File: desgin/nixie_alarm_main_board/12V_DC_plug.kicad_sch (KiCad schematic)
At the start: 4 parts, among them J1 DCPLUG 2x6.4mm 2A

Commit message: new caps footprint
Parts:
- C22: footprint GRM033D70J224ME01D -> Capacitor_SMD:C_0805_2012Metric_Pad1.18x1.45mm_HandSolder
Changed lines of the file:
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@@
 			)
 		)
-		(property "Footprint" "GRM033D70J224ME01D"
+		(property "Footprint" "Capacitor_SMD:C_0805_2012Metric_Pad1.18x1.45mm_HandSolder"
 			(at 282.372 81.534 0)
 			(effects

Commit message: new board v1
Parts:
- removed J1: DCPLUG 2x6.4mm 2A, DCJ20005AK1A, symbol SamacSys_Parts:DCJ200-05-A-K1-A
- added J1: PJ-094H-SMT-TR, PJ094HSMTTR, symbol SamacSys_Parts:PJ-094H-SMT-TR
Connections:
- net +12V: now also J1.1
- net GND: now also J1.2, J1.3
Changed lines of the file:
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@@
-	)
-	(junction
-		(at 104.14 93.472)
-		(diameter 0)
-		(color 0 0 0 0)
 	)
 	(junction
@@
 	)
 	(junction
-		(at 105.41 70.612)
+		(at 103.886 86.106)
 		(diameter 0)
 		(color 0 0 0 0)
@@
 	(wire
 		(pts
+			(xy 102.87 70.612) (xy 102.87 81.026)
+		)
+		(stroke
+			(width 0)
+			(type default)
+		)
+	)
+	(wire
+		(pts
 			(xy 143.002 70.612) (xy 143.002 77.978)
 		)
@@
 	(wire
 		(pts
-			(xy 102.87 70.612) (xy 105.41 70.612)
-		)
-		(stroke
-			(width 0)
-			(type default)
-		)
-	)
-	(wire
-		(pts
-			(xy 105.41 70.612) (xy 143.002 70.612)
+			(xy 102.87 70.612) (xy 143.002 70.612)
+		)
+		(stroke
+			(width 0)
+			(type default)
+		)
+	)
+	(wire
+		(pts
+			(xy 102.87 81.026) (xy 103.886 81.026)
 		)
 		(stroke
@@
 	(wire
 		(pts
-			(xy 104.14 93.472) (xy 105.41 93.472)
+			(xy 103.886 83.566) (xy 103.886 86.106)
 		)
 		(stroke
@@
 	(wire
 		(pts
+			(xy 103.886 86.106) (xy 103.886 93.472)
+		)
+		(stroke
+			(width 0)
+			(type default)
+		)
+	)
+	(wire
+		(pts
 			(xy 165.1 70.612) (xy 143.002 70.612)
 		)
@@
 		(pts
 			(xy 186.182 90.424) (xy 186.182 104.14)
-		)
-		(stroke
-			(width 0)
-			(type default)
-		)
-	)
-	(wire
-		(pts
-			(xy 102.87 93.472) (xy 104.14 93.472)
 		)
 		(stroke
@@
 	)
 	(symbol
-		(lib_id "SamacSys_Parts:DCJ200-05-A-K1-A")
-		(at 105.41 70.612 270)
-		(unit 1)
-		(exclude_from_sim no)
-		(in_bom yes)
-		(on_board yes)
-		(dnp no)
-		(fields_autoplaced yes)
-		(property "Reference" "J1"
-			(at 109.22 80.7719 90)
-			(effects
-				(font
-					(size 1.27 1.27)
-				)
-				(justify left)
-			)
-		)
-		(property "Value" "DCPLUG 2x6.4mm 2A"
-			(at 109.22 83.3119 90)
-			(effects
-				(font
-					(size 1.27 1.27)
-				)
-				(justify left)
-			)
-		)
-		(property "Footprint" "DCJ20005AK1A"
-			(at 10.49 89.662 0)
-			(effects
-				(font
-					(size 1.27 1.27)
-				)
-				(justify left top)
-				(hide yes)
-			)
-		)
-		(property "Datasheet" "https://componentsearchengine.com/Datasheets/2/DCJ200-05-A-K1-A.pdf"
-			(at -89.51 89.662 0)
-			(effects
-				(font
-					(size 1.27 1.27)
-				)
-				(justify left top)
-				(hide yes)
-			)
-		)
-		(property "Description" "DCJ200 Series 20 V 5 A 2 Conductors/3 Contacts Horizontal SMT DC Power Jack"
-			(at 105.41 70.612 0)
-			(effects
-				(font
-					(size 1.27 1.27)
-				)
-				(hide yes)
-			)
-		)
-		(property "Height" "11.3"
-			(at -289.51 89.662 0)
-			(effects
-				(font
-					(size 1.27 1.27)
-				)
-				(justify left top)
-				(hide yes)
-			)
-		)
-		(property "Mouser Part Number" "640-DCJ200-05-A-K1-A"
-			(at -389.51 89.662 0)
-			(effects
-				(font
-					(size 1.27 1.27)
-				)
-				(justify left top)
-				(hide yes)
-			)
-		)
-		(property "Mouser Price/Stock" "https://www.mouser.co.uk/ProductDetail/GCT/DCJ200-05-A-K1-A?qs=KUoIvG%2F9IlZdgC%252BD5EAHVw%3D%3D"
-			(at -489.51 89.662 0)
-			(effects
-				(font
-					(size 1.27 1.27)
-				)
-				(justify left top)
-				(hide yes)
-			)
-		)
-		(property "Manufacturer_Name" "GCT (GLOBAL CONNECTOR TECHNOLOGY)"
-			(at -589.51 89.662 0)
-			(effects
-				(font
-					(size 1.27 1.27)
-				)
-				(justify left top)
-				(hide yes)
-			)
-		)
-		(property "Manufacturer_Part_Number" "DCJ200-05-A-K1-A"
-			(at -689.51 89.662 0)
-			(effects
-				(font
-					(size 1.27 1.27)
-				)
-				(justify left top)
-				(hide yes)
-			)
-		)
-		(pin "2"
-		)
-		(pin "4"
-		)
-		(pin "3"
-		)
-		(pin "1"
-		)
-		(instances
-			(project "nixie_alarm_main_board"
-				(path "/a0d555d7-39a0-4a98-b831-70d97d0aa5a1/3f162d9f-7cb0-459b-831b-ac42fb433594"
-					(reference "J1")
-					(unit 1)
-				)
-			)
-		)
-	)
-	(symbol
 		(lib_id "power:GND")
 		(at 186.182 104.14 0)
@@
 	)
 	(symbol
+		(lib_id "SamacSys_Parts:PJ-094H-SMT-TR")
+		(at 103.886 81.026 0)
+		(unit 1)
+		(exclude_from_sim no)
+		(in_bom yes)
+		(on_board yes)
+		(dnp no)
+		(fields_autoplaced yes)
+		(property "Reference" "J1"
+			(at 115.316 73.914 0)
+			(effects
+				(font
+					(size 1.27 1.27)
+				)
+			)
+		)
+		(property "Value" "PJ-094H-SMT-TR"
+			(at 115.316 76.454 0)
+			(effects
+				(font
+					(size 1.27 1.27)
+				)
+			)
+		)
+		(property "Footprint" "PJ094HSMTTR"
+			(at 122.936 175.946 0)
+			(effects
+				(font
+					(size 1.27 1.27)
+				)
+				(justify left top)
+				(hide yes)
+			)
+		)
+		(property "Datasheet" "https://www.cuidevices.com/product/resource/digikeypdf/pj-094h-smt-tr.pdf"
+			(at 122.936 275.946 0)
+			(effects
+				(font
+					(size 1.27 1.27)
+				)
+				(justify left top)
+				(hide yes)
+			)
+		)
+		(property "Description" "DC Power Connectors power jack, 0.65 x 2.75 mm, horizontal, SMT, high current, 1 switch, w/ shielding, T&R package"
+			(at 103.886 81.026 0)
+			(effects
+				(font
+					(size 1.27 1.27)
+				)
+				(hide yes)
+			)
+		)
+		(property "Height" "3.7"
+			(at 122.936 475.946 0)
+			(effects
+				(font
+					(size 1.27 1.27)
+				)
+				(justify left top)
+				(hide yes)
+			)
+		)
+		(property "Mouser Part Number" "490-PJ-094H-SMT-TR"
+			(at 122.936 575.946 0)
+			(effects
+				(font
+					(size 1.27 1.27)
+				)
+				(justify left top)
+				(hide yes)
+			)
+		)
+		(property "Mouser Price/Stock" "https://www.mouser.co.uk/ProductDetail/CUI-Devices/PJ-094H-SMT-TR?qs=l7cgNqFNU1iCmsfPShkP7A%3D%3D"
+			(at 122.936 675.946 0)
+			(effects
+				(font
+					(size 1.27 1.27)
+				)
+				(justify left top)
+				(hide yes)
+			)
+		)
+		(property "Manufacturer_Name" "Same Sky"
+			(at 122.936 775.946 0)
+			(effects
+				(font
+					(size 1.27 1.27)
+				)
+				(justify left top)
+				(hide yes)
+			)
+		)
+		(property "Manufacturer_Part_Number" "PJ-094H-SMT-TR"
+			(at 122.936 875.946 0)
+			(effects
+				(font
+					(size 1.27 1.27)
+				)
+				(justify left top)
+				(hide yes)
+			)
+		)
+		(pin "1"
+		)
+		(pin "2"
+		)
+		(pin "MP1"
+		)
+		(pin "3"
+		)
+		(pin "MP2"
+		)
+		(instances
+			(project "nixie_alarm_main_board"
+				(path "/a0d555d7-39a0-4a98-b831-70d97d0aa5a1/3f162d9f-7cb0-459b-831b-ac42fb433594"
+					(reference "J1")
+					(unit 1)
+				)
+			)
+		)
+	)
+	(symbol
 		(lib_id "power:GND")
 		(at 143.002 104.14 0)
@@
 	(symbol
 		(lib_id "power:GND")
-		(at 104.14 93.472 0)
+		(at 103.886 93.472 0)
 		(unit 1)
 		(exclude_from_sim no)
@@
 		(fields_autoplaced yes)
 		(property "Reference" "#PWR050"
-			(at 104.14 99.822 0)
+			(at 103.886 99.822 0)
 			(effects
 				(font
@@
 		)
 		(property "Value" "GND"
-			(at 104.14 98.552 0)
+			(at 103.886 98.552 0)
 			(effects
 				(font
@@
 		)
 		(property "Footprint" ""
-			(at 104.14 93.472 0)
+			(at 103.886 93.472 0)
 			(effects
 				(font
@@
 		)
 		(property "Datasheet" ""
-			(at 104.14 93.472 0)
+			(at 103.886 93.472 0)
 			(effects
 				(font
@@
 		)
 		(property "Description" "Power symbol creates a global label with name \"GND\" , ground"
-			(at 104.14 93.472 0)
-			(effects
-				(font
+			(at 103.886 93.472 0)
+			(effects
+				(font

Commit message: little fixes
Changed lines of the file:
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@@
 		(fields_autoplaced yes)
 		(property "Reference" "J1"
-			(at 115.316 73.914 0)
+			(at 115.316 73.66 0)
 			(effects
 				(font
@@
 		)
 		(property "Value" "PJ-094H-SMT-TR"
-			(at 115.316 76.454 0)
+			(at 115.316 76.2 0)
 			(effects
 				(font

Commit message: tvs protection try
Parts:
- added D4: PUSB3AB4Z, SON50P100X250X50-10N, symbol SamacSys_Parts:PUSB3AB4Z
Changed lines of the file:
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@@
+	)
+	(symbol
+		(lib_id "SamacSys_Parts:PUSB3AB4Z")
+		(at 93.726 113.538 0)
+		(unit 1)
+		(exclude_from_sim no)
+		(in_bom yes)
+		(on_board yes)
+		(dnp no)
+		(fields_autoplaced yes)
+		(property "Reference" "D4"
+			(at 110.236 105.41 0)
+			(effects
+				(font
+					(size 1.27 1.27)
+				)
+			)
+		)
+		(property "Value" "PUSB3AB4Z"
+			(at 110.236 107.95 0)
+			(effects
+				(font
+					(size 1.27 1.27)
+				)
+			)
+		)
+		(property "Footprint" "SON50P100X250X50-10N"
+			(at 122.936 208.458 0)
+			(effects
+				(font
+					(size 1.27 1.27)
+				)
+				(justify left top)
+				(hide yes)
+			)
+		)
+		(property "Datasheet" "https://assets.nexperia.com/documents/data-sheet/PUSB3AB4.pdf"
+			(at 122.936 308.458 0)
+			(effects
+				(font
+					(size 1.27 1.27)
+				)
+				(justify left top)
+				(hide yes)
+			)
+		)
+		(property "Description" "PUSB3AB4 - ESD protection for ultra high-speed interfaces"
+			(at 93.726 113.538 0)
+			(effects
+				(font
+					(size 1.27 1.27)
+				)
+				(hide yes)
+			)
+		)
+		(property "Height" "0.5"
+			(at 122.936 508.458 0)
+			(effects
+				(font
+					(size 1.27 1.27)
+				)
+				(justify left top)
+				(hide yes)
+			)
+		)
+		(property "Mouser Part Number" "771-PUSB3AB4Z"
+			(at 122.936 608.458 0)
+			(effects
+				(font
+					(size 1.27 1.27)
+				)
+				(justify left top)
+				(hide yes)
+			)
+		)
+		(property "Mouser Price/Stock" "https://www.mouser.co.uk/ProductDetail/Nexperia/PUSB3AB4Z?qs=sPdA%252BpIfi%2F%252BQqDUUBPFV5w%3D%3D"
+			(at 122.936 708.458 0)
+			(effects
+				(font
+					(size 1.27 1.27)
+				)
+				(justify left top)
+				(hide yes)
+			)
+		)
+		(property "Manufacturer_Name" "Nexperia"
+			(at 122.936 808.458 0)
+			(effects
+				(font
+					(size 1.27 1.27)
+				)
+				(justify left top)
+				(hide yes)
+			)
+		)
+		(property "Manufacturer_Part_Number" "PUSB3AB4Z"
+			(at 122.936 908.458 0)
+			(effects
+				(font
+					(size 1.27 1.27)
+				)
+				(justify left top)
+				(hide yes)
+			)
+		)
+		(pin "10"
+		)
+		(pin "2"
+		)
+		(pin "5"
+		)
+		(pin "7"
+		)
+		(pin "3"
+		)
+		(pin "1"
+		)
+		(pin "6"
+		)
+		(pin "4"
+		)
+		(pin "8"
+		)
+		(pin "9"
+		)
+		(instances
+			(project "nixie_alarm_main_board"
+				(path "/a0d555d7-39a0-4a98-b831-70d97d0aa5a1/3f162d9f-7cb0-459b-831b-ac42fb433594"
+					(reference "D4")
+					(unit 1)
+				)
+			)
+		)
 	)
 	(symbol

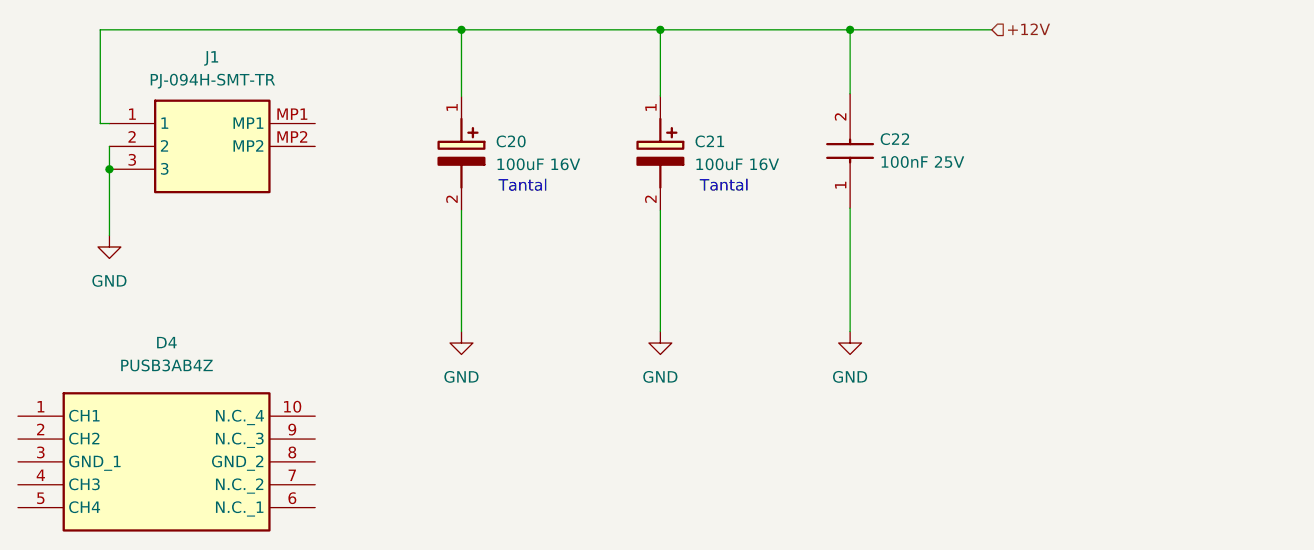
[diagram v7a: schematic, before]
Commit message: tvs added
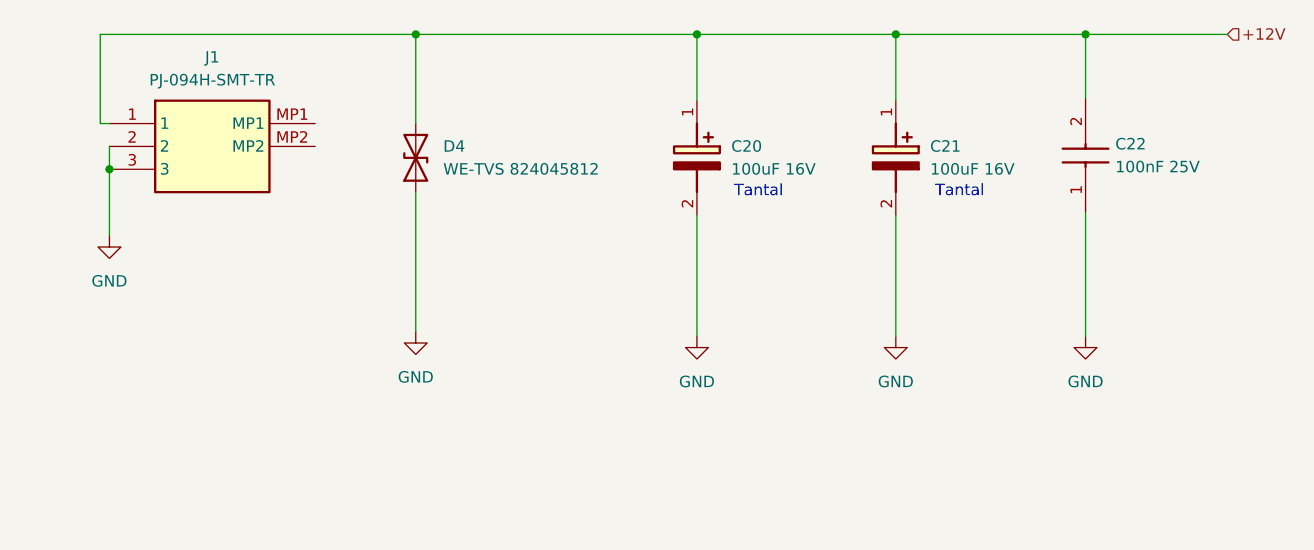
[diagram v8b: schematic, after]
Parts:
- removed D4: PUSB3AB4Z, SON50P100X250X50-10N, symbol SamacSys_Parts:PUSB3AB4Z
- added D4: WE-TVS 824045812, nixie:DFN-1610-2, symbol Device:D_TVS
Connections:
- net +12V: now also D4.2 (A2)
- net GND: now also D4.1 (A1)
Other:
- moved on the sheet: C20, C21, C22
